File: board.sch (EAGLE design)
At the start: 13 parts

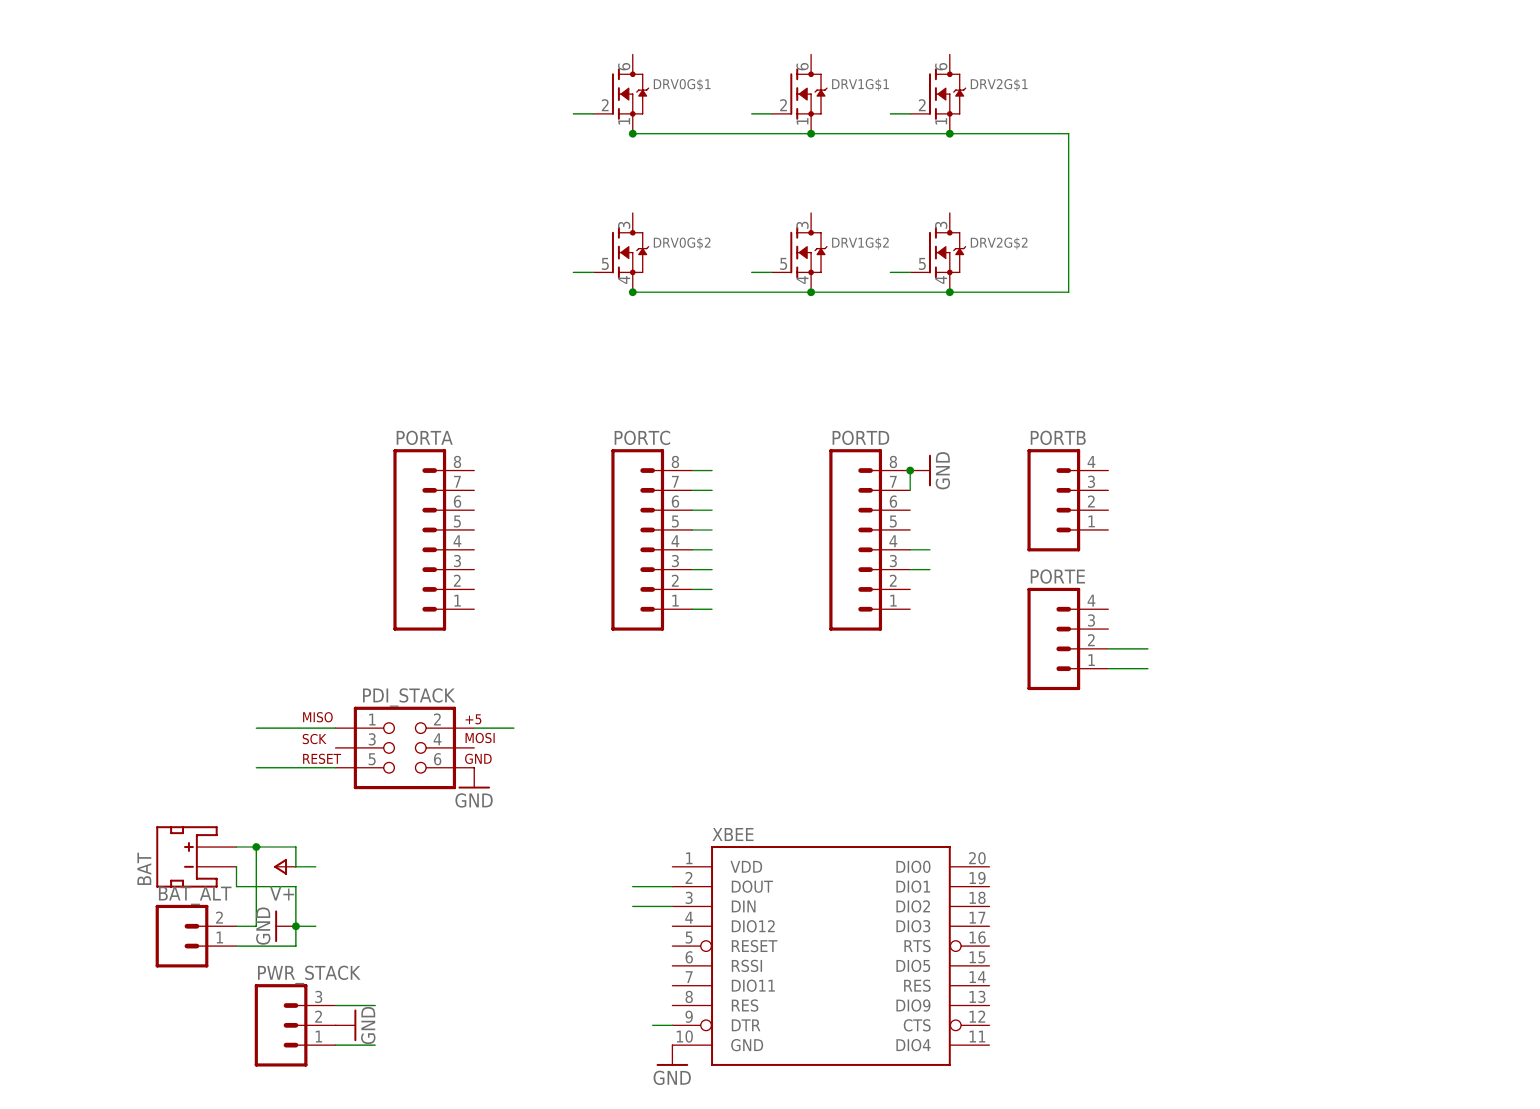
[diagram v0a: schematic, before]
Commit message: placed the led drivers and connectors
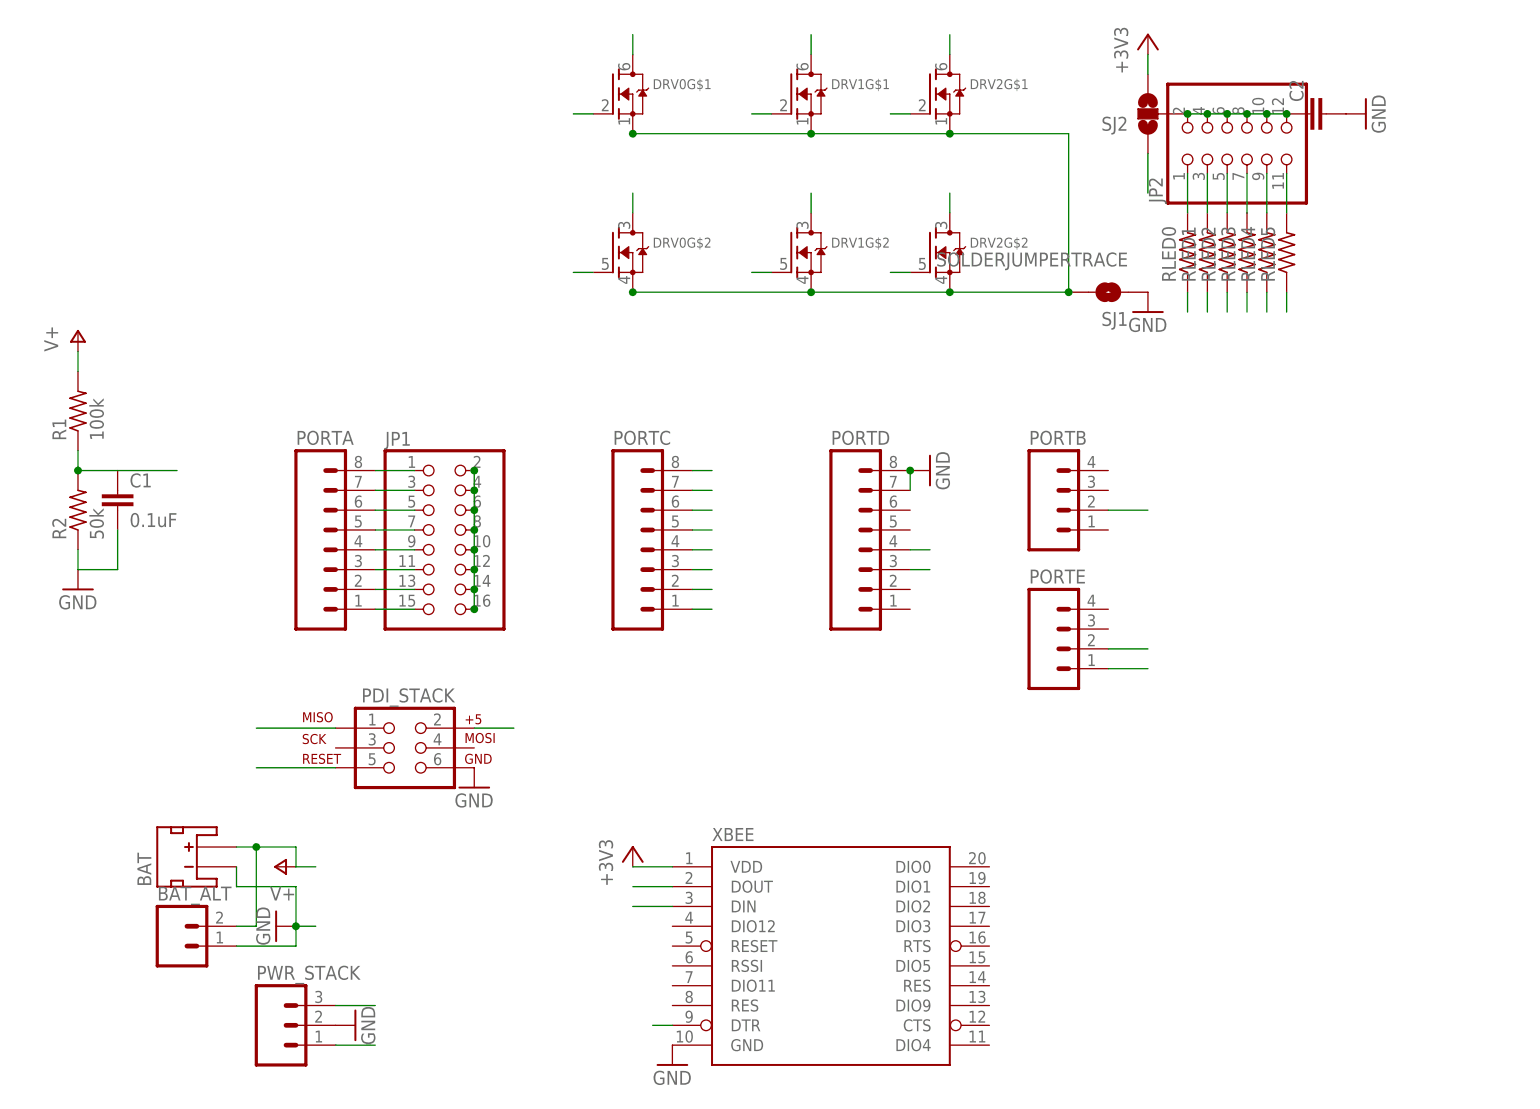
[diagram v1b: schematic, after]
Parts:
- added C1: 0.1uF, rcl:C-EUC0603K
- added C2: (no value), resistor:C-EUC0805K
- added JP1: (no value), pinhead:PINHD-2X8
- added JP2: (no value), pinhead:PINHD-2X6
- added R1: 100k, rcl:R-US_R0805
- added R2: 50k, rcl:R-US_R0805
- added RLED0, RLED1, RLED2, RLED3, RLED4, RLED5: (no value), resistor:R-US_R0805
- added SJ1: SOLDERJUMPERTRACE, SparkFun-Passives:SOLDERJUMPERTRACE
- added SJ2: (no value), SparkFun-Passives:SOLDERJUMPER_2WAY-OLDT
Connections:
- new net +3V3: SJ2.3, XBEE.VDD
- new net AGND: JP1.10, JP1.12, JP1.14, JP1.16, JP1.2, JP1.4, JP1.6, JP1.8
- new net LED0: DRV0G$1.D, RLED0.1
- new net LED0R: JP2.1, RLED0.2
- new net LED1: DRV0G$2.D, RLED1.1
- new net LED1R: JP2.3, RLED1.2
- new net LED2: DRV1G$1.D, RLED2.1
- new net LED2R: JP2.5, RLED2.2
- new net LED3: DRV1G$2.D, RLED3.1
- new net LED3R: JP2.7, RLED3.2
- new net LED4: DRV2G$1.D, RLED4.1
- new net LED4R: JP2.9, RLED4.2
- new net LED5: DRV2G$2.D, RLED5.1
- new net LED5R: JP2.11, RLED5.2
- new net PA0: JP1.15, PORTA.1
- new net PA1: JP1.13, PORTA.2
- new net PA2: JP1.11, PORTA.3
- new net PA3: JP1.9, PORTA.4
- new net PA4: JP1.7, PORTA.5
- new net PA5: JP1.5, PORTA.6
- new net PA6: JP1.3, PORTA.7
- new net PA7: JP1.1, PORTA.8
- new net VBAT_SENSE: C1.1, PORTB.2, R1.1, R2.2
- new net VLED: C2.1, JP2.10, JP2.12, JP2.2, JP2.4, JP2.6, JP2.8, SJ2.2
- net GND: now also C1.2, C2.2, R2.1, SJ1.1
- net GND_PWR: now also SJ1.2
- net VBAT: now also R1.2, SJ2.1
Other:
- moved on the sheet: PORTA

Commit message: this header must be 90deg one, otherwise it will not fit under the xbee
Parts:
- removed JP2: (no value), pinhead:PINHD-2X6
- added JP3: (no value), pinhead:PINHD-2X6/90
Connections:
- net LED0R: now also JP3.1; no longer JP2.1
- net LED1R: now also JP3.3; no longer JP2.3
- net LED2R: now also JP3.5; no longer JP2.5
- net LED3R: now also JP3.7; no longer JP2.7
- net LED4R: now also JP3.9; no longer JP2.9
- net LED5R: now also JP3.11; no longer JP2.11
- net VLED: now also JP3.10, JP3.12, JP3.2, JP3.4, JP3.6, JP3.8; no longer JP2.10, JP2.12, JP2.2, JP2.4, JP2.6, JP2.8
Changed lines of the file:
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@@
 <part name="C1" library="rcl" deviceset="C-EU" device="C0603K" value="0.1uF"/>
 <part name="JP1" library="pinhead" deviceset="PINHD-2X8" device=""/>
-<part name="JP2" library="pinhead" deviceset="PINHD-2X6" device=""/>
 <part name="+3V1" library="supply1" deviceset="+3V3" device=""/>
 <part name="SJ2" library="SparkFun-Passives" deviceset="SOLDERJUMPER_2WAY-OLD" device="T"/>
@@
 <part name="SJ1" library="SparkFun-Passives" deviceset="SOLDERJUMPER" device="TRACE"/>
 <part name="GND8" library="supply1" deviceset="GND" device=""/>
+<part name="JP3" library="pinhead" deviceset="PINHD-2X6" device="/90"/>
 </parts>
 <sheets>
@@
 <instance part="C1" gate="G$1" x="-22.86" y="104.14"/>
 <instance part="JP1" gate="A" x="17.78" y="99.06"/>
-<instance part="JP2" gate="A" x="119.38" y="147.32" rot="R90"/>
 <instance part="+3V1" gate="G$1" x="109.22" y="162.56"/>
 <instance part="SJ2" gate="G$1" x="109.22" y="152.4" rot="R180"/>
@@
 <instance part="SJ1" gate="1" x="104.14" y="129.54" rot="R180"/>
 <instance part="GND8" gate="1" x="109.22" y="127"/>
+<instance part="JP3" gate="A" x="119.38" y="147.32" rot="R90"/>
 </instances>
 <busses>
@@
 <net name="VLED" class="0">
 <segment>
-<pinref part="JP2" gate="A" pin="12"/>
-<pinref part="JP2" gate="A" pin="2"/>
 <wire x1="127" y1="152.4" x2="124.46" y2="152.4" width="0.1524" layer="91"/>
+<pinref part="SJ2" gate="G$1" pin="2"/>
+<pinref part="C2" gate="G$1" pin="1"/>
+<pinref part="JP3" gate="A" pin="2"/>
+<junction x="114.3" y="152.4"/>
+<pinref part="JP3" gate="A" pin="4"/>
+<wire x1="124.46" y1="152.4" x2="121.92" y2="152.4" width="0.1524" layer="91"/>
+<wire x1="121.92" y1="152.4" x2="119.38" y2="152.4" width="0.1524" layer="91"/>
+<wire x1="119.38" y1="152.4" x2="116.84" y2="152.4" width="0.1524" layer="91"/>
+<wire x1="116.84" y1="152.4" x2="114.3" y2="152.4" width="0.1524" layer="91"/>
+<junction x="116.84" y="152.4"/>
+<pinref part="JP3" gate="A" pin="6"/>
+<junction x="119.38" y="152.4"/>
+<pinref part="JP3" gate="A" pin="8"/>
+<junction x="121.92" y="152.4"/>
+<pinref part="JP3" gate="A" pin="10"/>
+<junction x="124.46" y="152.4"/>
+<pinref part="JP3" gate="A" pin="12"/>
 <junction x="127" y="152.4"/>
-<pinref part="JP2" gate="A" pin="10"/>
-<junction x="124.46" y="152.4"/>
-<wire x1="124.46" y1="152.4" x2="121.92" y2="152.4" width="0.1524" layer="91"/>
-<pinref part="JP2" gate="A" pin="8"/>
-<junction x="121.92" y="152.4"/>
-<wire x1="121.92" y1="152.4" x2="119.38" y2="152.4" width="0.1524" layer="91"/>
-<pinref part="JP2" gate="A" pin="6"/>
-<junction x="119.38" y="152.4"/>
-<wire x1="119.38" y1="152.4" x2="116.84" y2="152.4" width="0.1524" layer="91"/>
-<pinref part="JP2" gate="A" pin="4"/>
-<junction x="116.84" y="152.4"/>
-<wire x1="116.84" y1="152.4" x2="114.3" y2="152.4" width="0.1524" layer="91"/>
-<pinref part="SJ2" gate="G$1" pin="2"/>
-<junction x="114.3" y="152.4"/>
-<pinref part="C2" gate="G$1" pin="1"/>
 </segment>
 </net>
@@
 <net name="LED0R" class="1">
 <segment>
-<pinref part="JP2" gate="A" pin="1"/>
 <pinref part="RLED0" gate="G$1" pin="2"/>
 <wire x1="114.3" y1="139.7" x2="114.3" y2="144.78" width="0.1524" layer="91"/>
+<pinref part="JP3" gate="A" pin="1"/>
 </segment>
 </net>
 <net name="LED1R" class="1">
 <segment>
-<pinref part="JP2" gate="A" pin="3"/>
 <pinref part="RLED1" gate="G$1" pin="2"/>
 <wire x1="116.84" y1="139.7" x2="116.84" y2="144.78" width="0.1524" layer="91"/>
+<pinref part="JP3" gate="A" pin="3"/>
 </segment>
 </net>
 <net name="LED2R" class="1">
 <segment>
-<pinref part="JP2" gate="A" pin="5"/>
 <pinref part="RLED2" gate="G$1" pin="2"/>
 <wire x1="119.38" y1="139.7" x2="119.38" y2="144.78" width="0.1524" layer="91"/>
+<pinref part="JP3" gate="A" pin="5"/>
 </segment>
 </net>
 <net name="LED3R" class="1">
 <segment>
-<pinref part="JP2" gate="A" pin="7"/>
 <pinref part="RLED3" gate="G$1" pin="2"/>
 <wire x1="121.92" y1="139.7" x2="121.92" y2="144.78" width="0.1524" layer="91"/>
+<pinref part="JP3" gate="A" pin="7"/>
 </segment>
 </net>
 <net name="LED4R" class="1">
 <segment>
-<pinref part="JP2" gate="A" pin="9"/>
 <pinref part="RLED4" gate="G$1" pin="2"/>
 <wire x1="124.46" y1="139.7" x2="124.46" y2="144.78" width="0.1524" layer="91"/>
+<pinref part="JP3" gate="A" pin="9"/>
 </segment>
 </net>
 <net name="LED5R" class="1">
 <segment>
-<pinref part="JP2" gate="A" pin="11"/>
 <pinref part="RLED5" gate="G$1" pin="2"/>
 <wire x1="127" y1="139.7" x2="127" y2="144.78" width="0.1524" layer="91"/>
-</segment>
-</net>
+<pinref part="JP3" gate="A" pin="11"/>
+</segment>
+</net>
